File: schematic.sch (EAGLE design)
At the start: 58 parts, among them J1 FTDI_DEVICERA_SMT, M1 WIRELESS-NRF24L01, U1 ATMEGA328P_TQFP, U2 GY-521MPU6050, U3 TPS63060, Y1 8Mhz

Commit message: Updated parts to reflect actual selection
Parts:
- removed L2: (no value), coilcraft:INDUCTOR.XAL4020
- removed R14: 100, resistor:R-US_M2309
- removed Y1: 8Mhz, quad:CRYSTALHC49US
- added Q1: 8MHz, crystal:CSM-7X-DU
- C1: value 0.1uF -> 100uF; device SparkFun-Capacitors:0.1UF-25V-5%(0603) -> rcl:C-USC1210
- C10, C9: value 22uF -> 0.1uF; device SparkFun-Passives:CAP0603-CAP -> rcl:C-USC0603
- C11: value 10uF -> 0.1uF; device SparkFun-Passives:CAP0603-CAP -> rcl:C-USC0603
- C12: value 100uF -> 0.1uF; device SparkFun-Passives:CAP0603-CAP -> rcl:C-USC0603
- C13: value 10uF -> 27pF; device SparkFun-Passives:CAP0603-CAP -> resistor:C-USC0603
- C14: value 100nF -> 27pF; device SparkFun-Passives:CAP0603-CAP -> resistor:C-USC0603
- C15: device SparkFun-Passives:CAP0603-CAP -> resistor:C-USC0201
- C16: value 26pF -> 10uF; device SparkFun-Capacitors:0.1UF-25V-5%(0603) -> resistor:C-USC0805K
- C17: value 26pF -> 0.1uF; device SparkFun-Capacitors:0.1UF-25V-5%(0603) -> resistor:C-USC0201
- C2, C3: value 0.1uF -> 10uF; device SparkFun-Capacitors:0.1UF-25V-5%(0603) -> resistor:C-USC0805K
- C4: device SparkFun-Capacitors:0.1UF-25V-5%(0603) -> rcl:C-USC0603
- C5: value 10uF -> 10pF; device SparkFun-Passives:CAP0603-CAP -> rcl:C-USC0603
- C6: value 10pF -> 22uF; device SparkFun-Passives:CAP0603-CAP -> rcl:C-USC0603
- C7: device SparkFun-Passives:CAP0603-CAP -> rcl:C-USC0603
- C8: value 0.1uF -> 22uF; device SparkFun-Passives:CAP0603-CAP -> rcl:C-USC0603
- L1: device rcl:L-USL1812 -> coilcraft:INDUCTOR.XAL4020
- LED1, LED2: device led:LED -> led:LEDSML0603
- LED3, LED4: value RED -> YELLOW
- R1: value 10K -> 820; device SparkFun-Resistors:10KOHM-1/10W-1%(0603)0603 -> rcl:R-US_R0603
- R10: value 5M -> 10K; device resistor:R-US_M2309 -> resistor:R-US_R0603
- R11: device resistor:R-US_M2309 -> resistor:R-US_R0603
- R13: value 100 -> 10K
- R2: value 100 -> 150K
- R3: value 100 -> 50K; device resistor:R-US_M2309 -> resistor:R-US_R0805
- R4: value 10K -> 560K; device resistor:R-US_M2309 -> rcl:R-US_R0805
- R5: value 10K -> 100K; device resistor:R-US_M2309 -> rcl:R-US_R0402
- R6: value 1.12M -> 820; device resistor:R-US_M2309 -> rcl:R-US_R0603
- R7: value 200K -> 10K; device resistor:R-US_M2309 -> resistor:R-US_R0603
- R8: value 1M -> 820; device resistor:R-US_M2309 -> rcl:R-US_R0603
- R9: value 15M -> 820; device resistor:R-US_M2309 -> rcl:R-US_R0603
- T1, T2, T3, T4: value N-CHANNEL-MOSFET-IRLML6244TRPBF -> NMOS
- renumbered U$11 to T4, U$12 to D4, U$2 to T1, U$3 to D1, U$5 to T2, U$6 to D2, U$8 to T3, U$9 to D3
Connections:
- removed net PG: R8.1, U3.PG
- net DEBUG_LED1: now also R9.2; no longer R13.2
- net DEBUG_LED2: now also R8.2; no longer R14.2
- net DTR: now also C9.1; no longer C1.1
- net GND: now also C1.2, C10.2, C11.2, C12.2, C13.2, C14.2, C15.2, C16.2, C17.2, C5.2, C6.2, C7.2, C8.2, R11.1, R13.2, R3.1, R5.1; no longer C10.1, C11.1, C12.1, C13.1, C14.1, C15.1, C16.1, C17.1, C5.1, C6.1, C7.1, C8.1, C9.1, R11.2, R4.2, R5.2, R7.1
- net N$1: now also C13.1, Q1.1; no longer C16.2, Y1.1
- net N$10: now also R1.2; no longer R2.1
- net N$11: now also R6.1; no longer R3.1
- net N$12: now also R9.1; no longer R13.1
- net N$13: now also R8.1; no longer R14.1
- net N$2: now also C9.2, R7.1; no longer C1.2, R1.1
- net N$25: now also C12.1; no longer C2.1
- net N$32: now also C5.1, R4.1, R5.2; no longer C6.2, R6.1, R7.2
- net N$33: now also C4.1; no longer C8.2
- net N$4: now also C14.1, Q1.2; no longer C17.2, Y1.2
- net PWM1: now also R10.2; no longer R4.1
- net PWM2: now also R11.2; no longer R5.1
- net PWM3: now also R12.1; no longer R11.1
- net PWM4: now also R13.1; no longer R12.1
- net VCC: now also C1.1, C2.1, C3.1, R1.1; no longer C11.2, C12.2, C5.2, R9.2
- net V_BAT: now also R2.1, R3.2; no longer R10.2, R9.1
- net V_REG_OUT: now also C10.1, C11.1, C15.1, C16.1, C17.1, C6.1, C7.1, C8.1, R4.2, R7.2; no longer C10.2, C13.2, C14.2, C15.2, C3.1, C4.1, C7.2, C9.2, R1.2, R3.2, R8.2
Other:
- moved on the sheet: C1, C10, C11, C12, C13, C14, C15, C16, C17, C2, C3, C4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

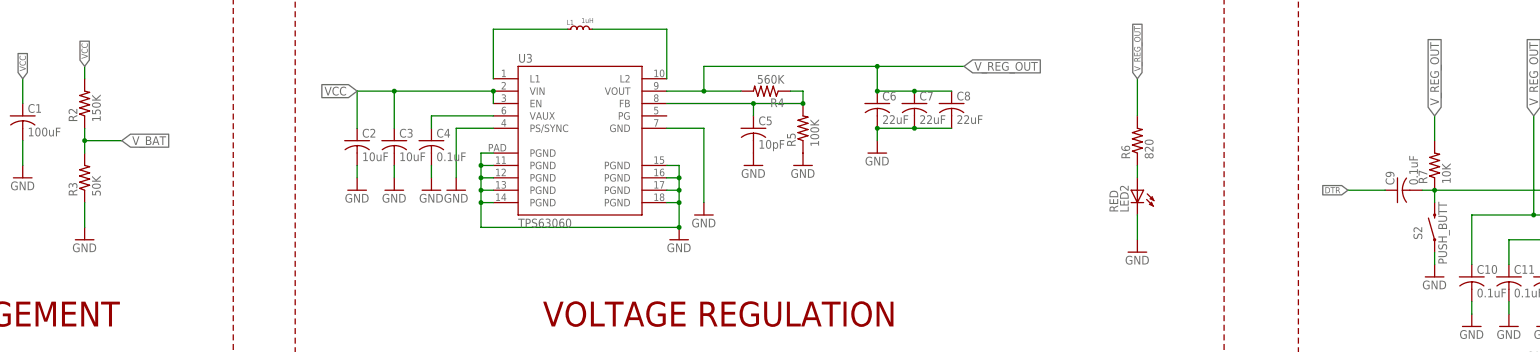
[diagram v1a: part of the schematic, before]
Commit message: Changed voltage divider values
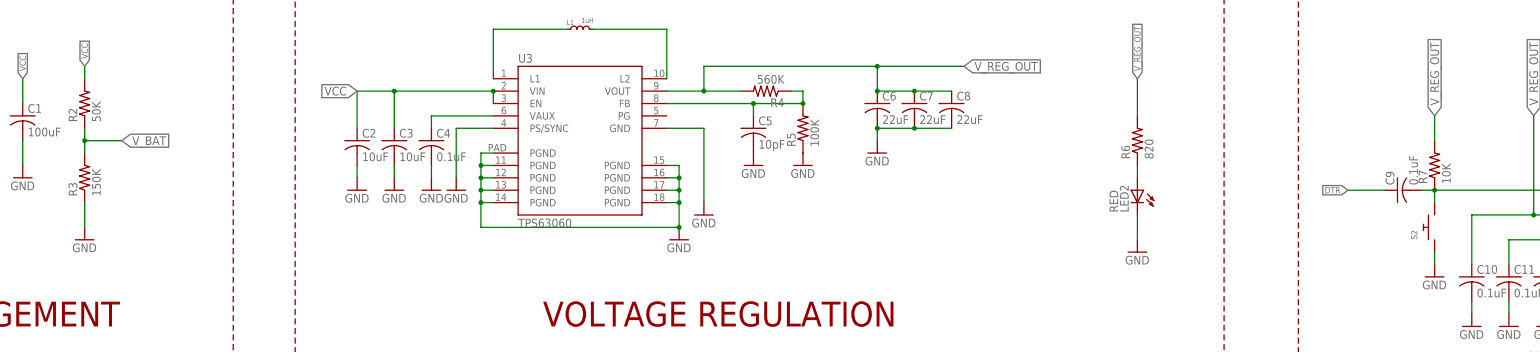
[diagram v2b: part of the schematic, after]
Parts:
- R2: value 150K -> 50K
- R3: value 50K -> 150K
- S2: value PUSH_BUTT -> (none); device quad:SWITCH-MOMENTARY-2SMD -> adafruit:SWITCH_PUSHBUTTONSOFTTOUCHSMD_SJ
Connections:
- net GND: now also S2.P$1; no longer S2.1
- net N$2: now also S2.P$2; no longer S2.2
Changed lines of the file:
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@@
 <part name="GND18" library="SparkFun" deviceset="GND" device=""/>
 <part name="GND19" library="SparkFun" deviceset="GND" device=""/>
-<part name="R2" library="resistor" library_urn="urn:adsk.eagle:library:348" deviceset="R-US_" device="M2309" package3d_urn="urn:adsk.eagle:package:26085/1" value="150K"/>
+<part name="R2" library="resistor" library_urn="urn:adsk.eagle:library:348" deviceset="R-US_" device="M2309" package3d_urn="urn:adsk.eagle:package:26085/1" value="50K"/>
 <part name="GND" library="SparkFun" deviceset="GND" device=""/>
 <part name="GND3" library="SparkFun" deviceset="GND" device=""/>
@@
 <part name="GND20" library="SparkFun" deviceset="GND" device=""/>
 <part name="U$1" library="quad" deviceset="JST_CONNECTOR_FEMALE" device=""/>
-<part name="S2" library="quad" deviceset="SWITCH-MOMENTARY-2" device="SMD" value="PUSH_BUTT"/>
 <part name="T1" library="quad" deviceset="N-CHANNEL-MOSFET" device="-IRLML6244TRPBF" value="NMOS"/>
 <part name="D1" library="quad" deviceset="DB2W40300L" device=""/>
@@
 <part name="C1" library="rcl" library_urn="urn:adsk.eagle:library:334" deviceset="C-US" device="C1210" package3d_urn="urn:adsk.eagle:package:23619/2" value="100uF"/>
 <part name="C17" library="resistor" library_urn="urn:adsk.eagle:library:348" deviceset="C-US" device="C0201" package3d_urn="urn:adsk.eagle:package:26209/1" value="0.1uF"/>
-<part name="R3" library="resistor" library_urn="urn:adsk.eagle:library:348" deviceset="R-US_" device="R0805" package3d_urn="urn:adsk.eagle:package:26059/1" value="50K"/>
+<part name="R3" library="resistor" library_urn="urn:adsk.eagle:library:348" deviceset="R-US_" device="R0805" package3d_urn="urn:adsk.eagle:package:26059/1" value="150K"/>
 <part name="C4" library="rcl" library_urn="urn:adsk.eagle:library:334" deviceset="C-US" device="C0603" package3d_urn="urn:adsk.eagle:package:23616/2" value="0.1uF"/>
 <part name="C9" library="rcl" library_urn="urn:adsk.eagle:library:334" deviceset="C-US" device="C0603" package3d_urn="urn:adsk.eagle:package:23616/2" value="0.1uF"/>
@@
 <part name="C8" library="rcl" library_urn="urn:adsk.eagle:library:334" deviceset="C-US" device="C0603" package3d_urn="urn:adsk.eagle:package:23616/2" value="22uF"/>
 <part name="C16" library="resistor" library_urn="urn:adsk.eagle:library:348" deviceset="C-US" device="C0805K" package3d_urn="urn:adsk.eagle:package:26201/1" value="10uF"/>
+<part name="S2" library="adafruit" deviceset="SWITCH_PUSHBUTTON" device="SOFTTOUCHSMD_SJ"/>
 </parts>
 <sheets>
@@
 <instance part="GND20" gate="1" x="15.24" y="12.7"/>
 <instance part="U$1" gate="G$1" x="-198.12" y="127" rot="MR270"/>
-<instance part="S2" gate="G$1" x="139.7" y="99.06" smashed="yes" rot="R90">
-<attribute name="NAME" x="137.16" y="96.52" size="1.778" layer="95" rot="R90"/>
-<attribute name="VALUE" x="142.24" y="91.44" size="1.778" layer="96" rot="R90"/>
-</instance>
 <instance part="T1" gate="G$1" x="-190.5" y="5.08"/>
 <instance part="D1" gate="G$1" x="-175.26" y="25.4" rot="R90"/>
@@
 <instance part="C8" gate="G$1" x="40.64" y="124.46"/>
 <instance part="C16" gate="G$1" x="0" y="-43.18"/>
+<instance part="S2" gate="G$1" x="139.7" y="99.06" rot="R90"/>
 </instances>
 <busses>
@@
 <wire x1="139.7" y1="106.68" x2="137.16" y2="106.68" width="0.1524" layer="91"/>
 <wire x1="139.7" y1="106.68" x2="139.7" y2="104.14" width="0.1524" layer="91"/>
-<pinref part="S2" gate="G$1" pin="2"/>
 <pinref part="R7" gate="G$1" pin="1"/>
 <pinref part="C9" gate="G$1" pin="2"/>
+<pinref part="S2" gate="G$1" pin="P$2"/>
 </segment>
 </net>
@@
 <pinref part="GND1" gate="1" pin="GND"/>
 <wire x1="139.7" y1="91.44" x2="139.7" y2="93.98" width="0.1524" layer="91"/>
-<pinref part="S2" gate="G$1" pin="1"/>
-</segment>
-<segment>
+<pinref part="S2" gate="G$1" pin="P$1"/>
+</segment>
+<segment>

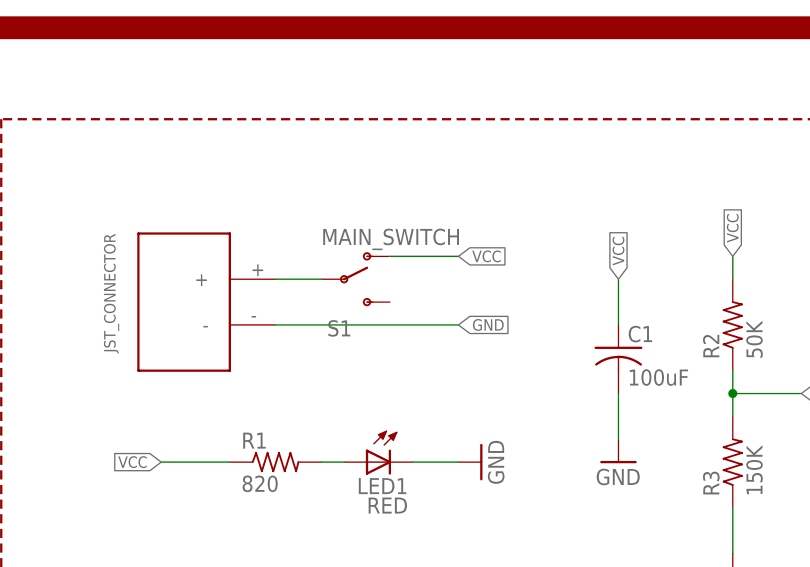
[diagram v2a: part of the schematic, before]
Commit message: added slide switch
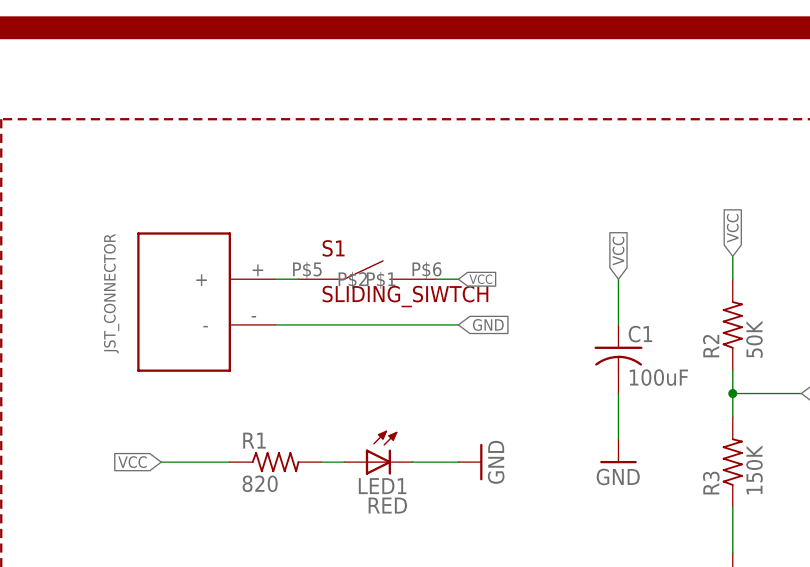
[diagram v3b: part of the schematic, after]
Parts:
- S1: value MAIN_SWITCH -> SLIDING_SIWTCH; device SparkFun:SWITCH-SPST-SMD-A -> wurth:SLIDING_SIWTCH
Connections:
- net N$8: now also S1.P$1; no longer S1.P
- net VCC: now also S1.P$2; no longer S1.O
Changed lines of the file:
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@@
 <layer number="59" name="tCarbon" color="7" fill="1" visible="no" active="no"/>
 <layer number="60" name="bCarbon" color="7" fill="1" visible="no" active="no"/>
+<layer number="88" name="SimResults" color="9" fill="1" visible="yes" active="yes"/>
+<layer number="89" name="SimProbes" color="9" fill="1" visible="yes" active="yes"/>
 <layer number="90" name="Modules" color="5" fill="1" visible="yes" active="yes"/>
 <layer number="91" name="Nets" color="2" fill="1" visible="yes" active="yes"/>
@@
 <part name="U$13" library="quad" deviceset="JST_CONNECTOR_FEMALE" device=""/>
 <part name="GND24" library="SparkFun" deviceset="GND" device=""/>
-<part name="S1" library="SparkFun" deviceset="SWITCH-SPST" device="-SMD-A" value="MAIN_SWITCH"/>
 <part name="GND4" library="SparkFun" deviceset="GND" device=""/>
 <part name="GND25" library="SparkFun" deviceset="GND" device=""/>
@@
 <part name="C16" library="resistor" library_urn="urn:adsk.eagle:library:348" deviceset="C-US" device="C0805K" package3d_urn="urn:adsk.eagle:package:26201/1" value="10uF"/>
 <part name="S2" library="adafruit" deviceset="SWITCH_PUSHBUTTON" device="SOFTTOUCHSMD_SJ"/>
+<part name="S1" library="wurth" deviceset="SLIDING_SIWTCH" device=""/>
 </parts>
 <sheets>
@@
 <instance part="U$13" gate="G$1" x="-152.4" y="-38.1" rot="MR270"/>
 <instance part="GND24" gate="1" x="-139.7" y="-71.12"/>
-<instance part="S1" gate="1" x="-180.34" y="129.54"/>
 <instance part="GND4" gate="1" x="-165.1" y="109.22" rot="R90"/>
 <instance part="GND25" gate="1" x="78.74" y="93.98"/>
@@
 <instance part="C16" gate="G$1" x="0" y="-43.18"/>
 <instance part="S2" gate="G$1" x="139.7" y="99.06" rot="R90"/>
+<instance part="S1" gate="G$1" x="-180.34" y="129.54" smashed="yes">
+<attribute name="NAME" x="-182.88" y="132.08" size="1.778" layer="94"/>
+<attribute name="VALUE" x="-182.88" y="127" size="1.778" layer="94"/>
+</instance>
 </instances>
 <busses>
@@
 </segment>
 <segment>
-<pinref part="S1" gate="1" pin="O"/>
-<wire x1="-175.26" y1="132.08" x2="-167.64" y2="132.08" width="0.1524" layer="91"/>
-<label x="-167.64" y="132.08" size="1.27" layer="95" xref="yes"/>
-</segment>
-<segment>
 <wire x1="-193.04" y1="109.22" x2="-200.66" y2="109.22" width="0.1524" layer="91"/>
 <label x="-200.66" y="109.22" size="1.27" layer="95" rot="R180" xref="yes"/>
 <pinref part="R1" gate="G$1" pin="1"/>
+</segment>
+<segment>
+<pinref part="S1" gate="G$1" pin="P$2"/>
+<wire x1="-170.18" y1="129.54" x2="-167.64" y2="129.54" width="0.1524" layer="91"/>
+<label x="-167.64" y="129.54" size="1.016" layer="95" xref="yes"/>
 </segment>
 </net>
@@
 </segment>
 </net>
-<net name="N$8" class="0">
-<segment>
-<pinref part="S1" gate="1" pin="P"/>
-<pinref part="U$1" gate="G$1" pin="+"/>
-<wire x1="-187.96" y1="129.54" x2="-182.88" y2="129.54" width="0.1524" layer="91"/>
-</segment>
-</net>
 <net name="N$10" class="0">
 <segment>
@@
 </segment>
 </net>
+<net name="N$8" class="0">
+<segment>
+<pinref part="U$1" gate="G$1" pin="+"/>
+<pinref part="S1" gate="G$1" pin="P$1"/>
+<wire x1="-187.96" y1="129.54" x2="-185.42" y2="129.54" width="0.1524" layer="91"/>
+</segment>
+</net>
